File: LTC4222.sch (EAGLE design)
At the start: 29 parts, among them IC1 67997-100HLF, IC2 LTC4222, J1 PMV15ENEAR, J2 PMV15ENEAR

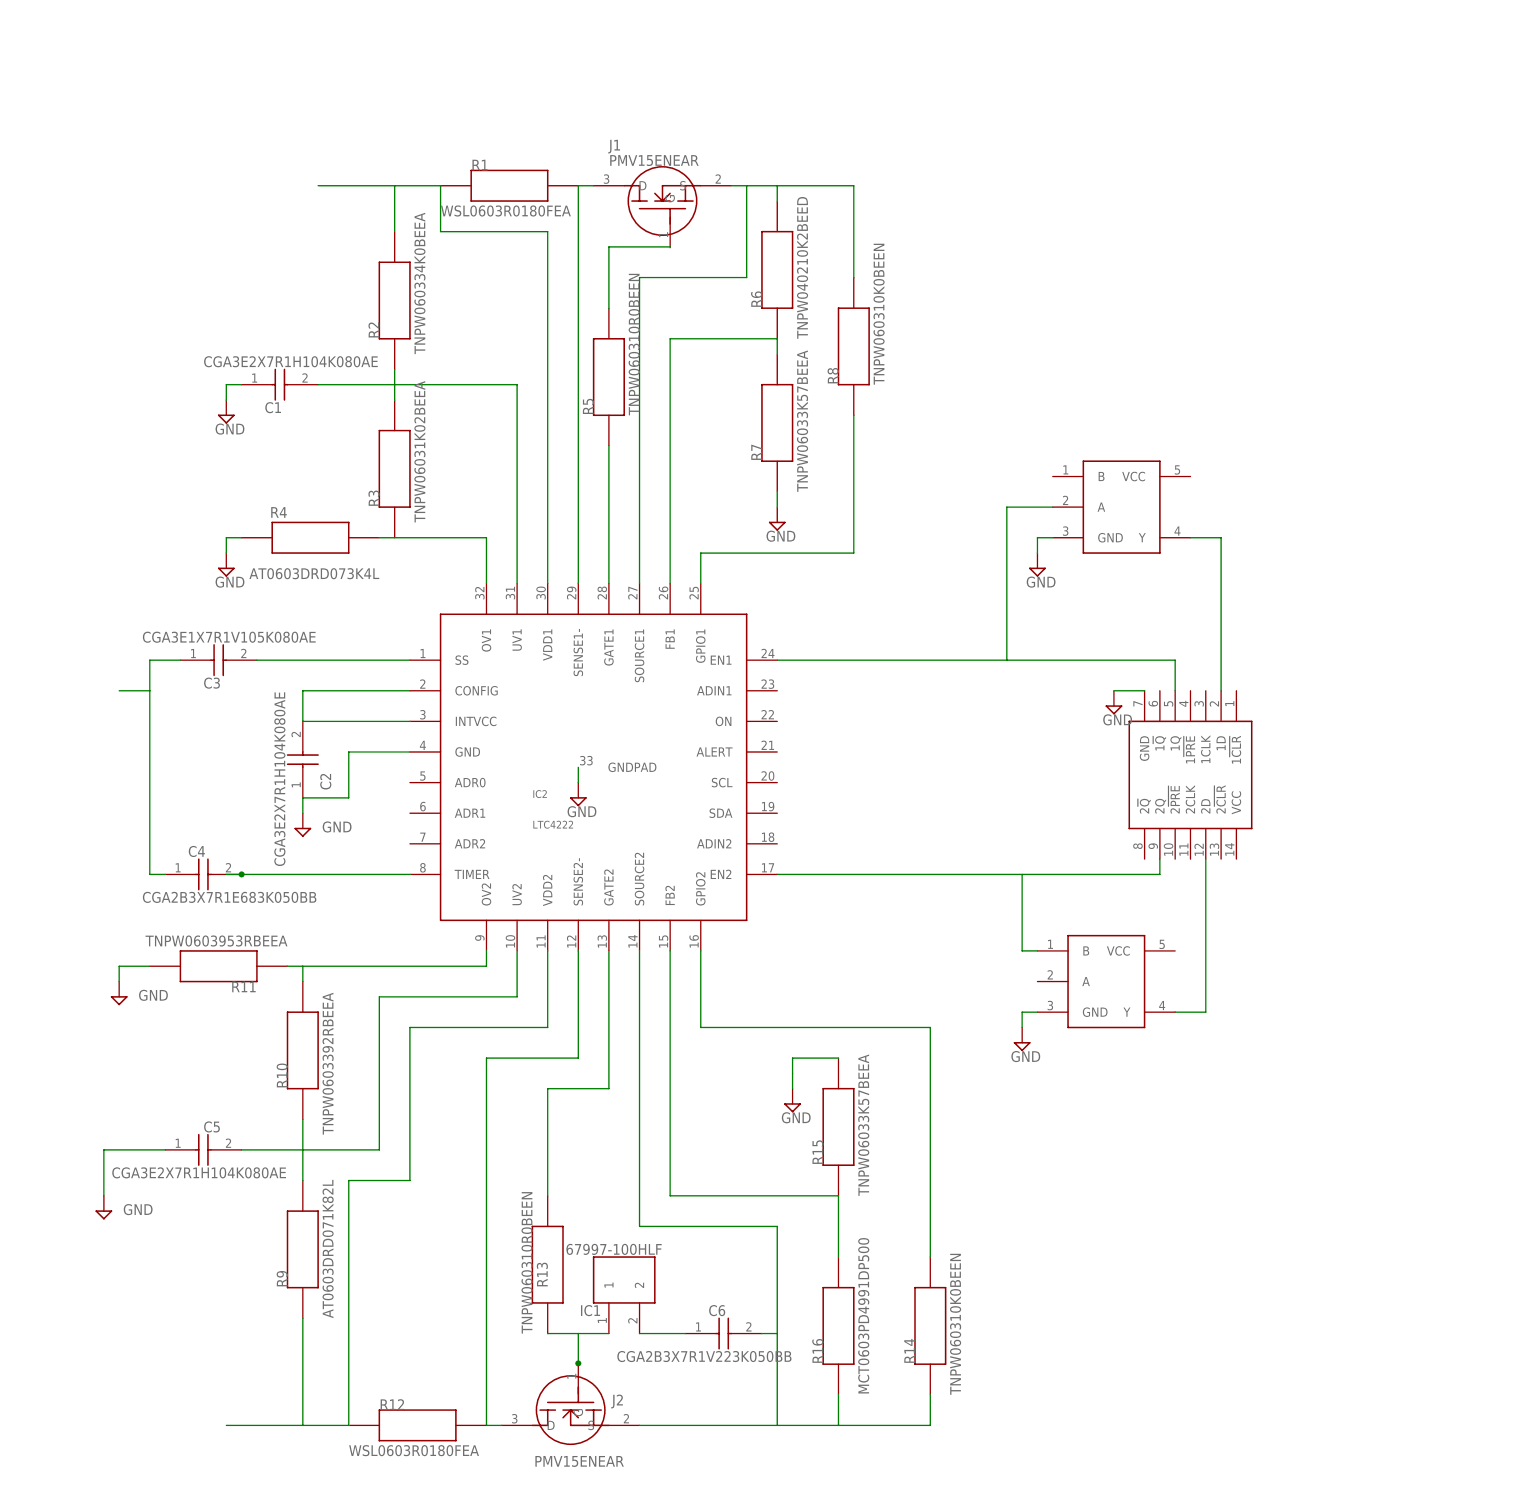
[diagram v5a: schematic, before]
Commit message: Polished LTC4222 schematic and added test points. Started on pin heads
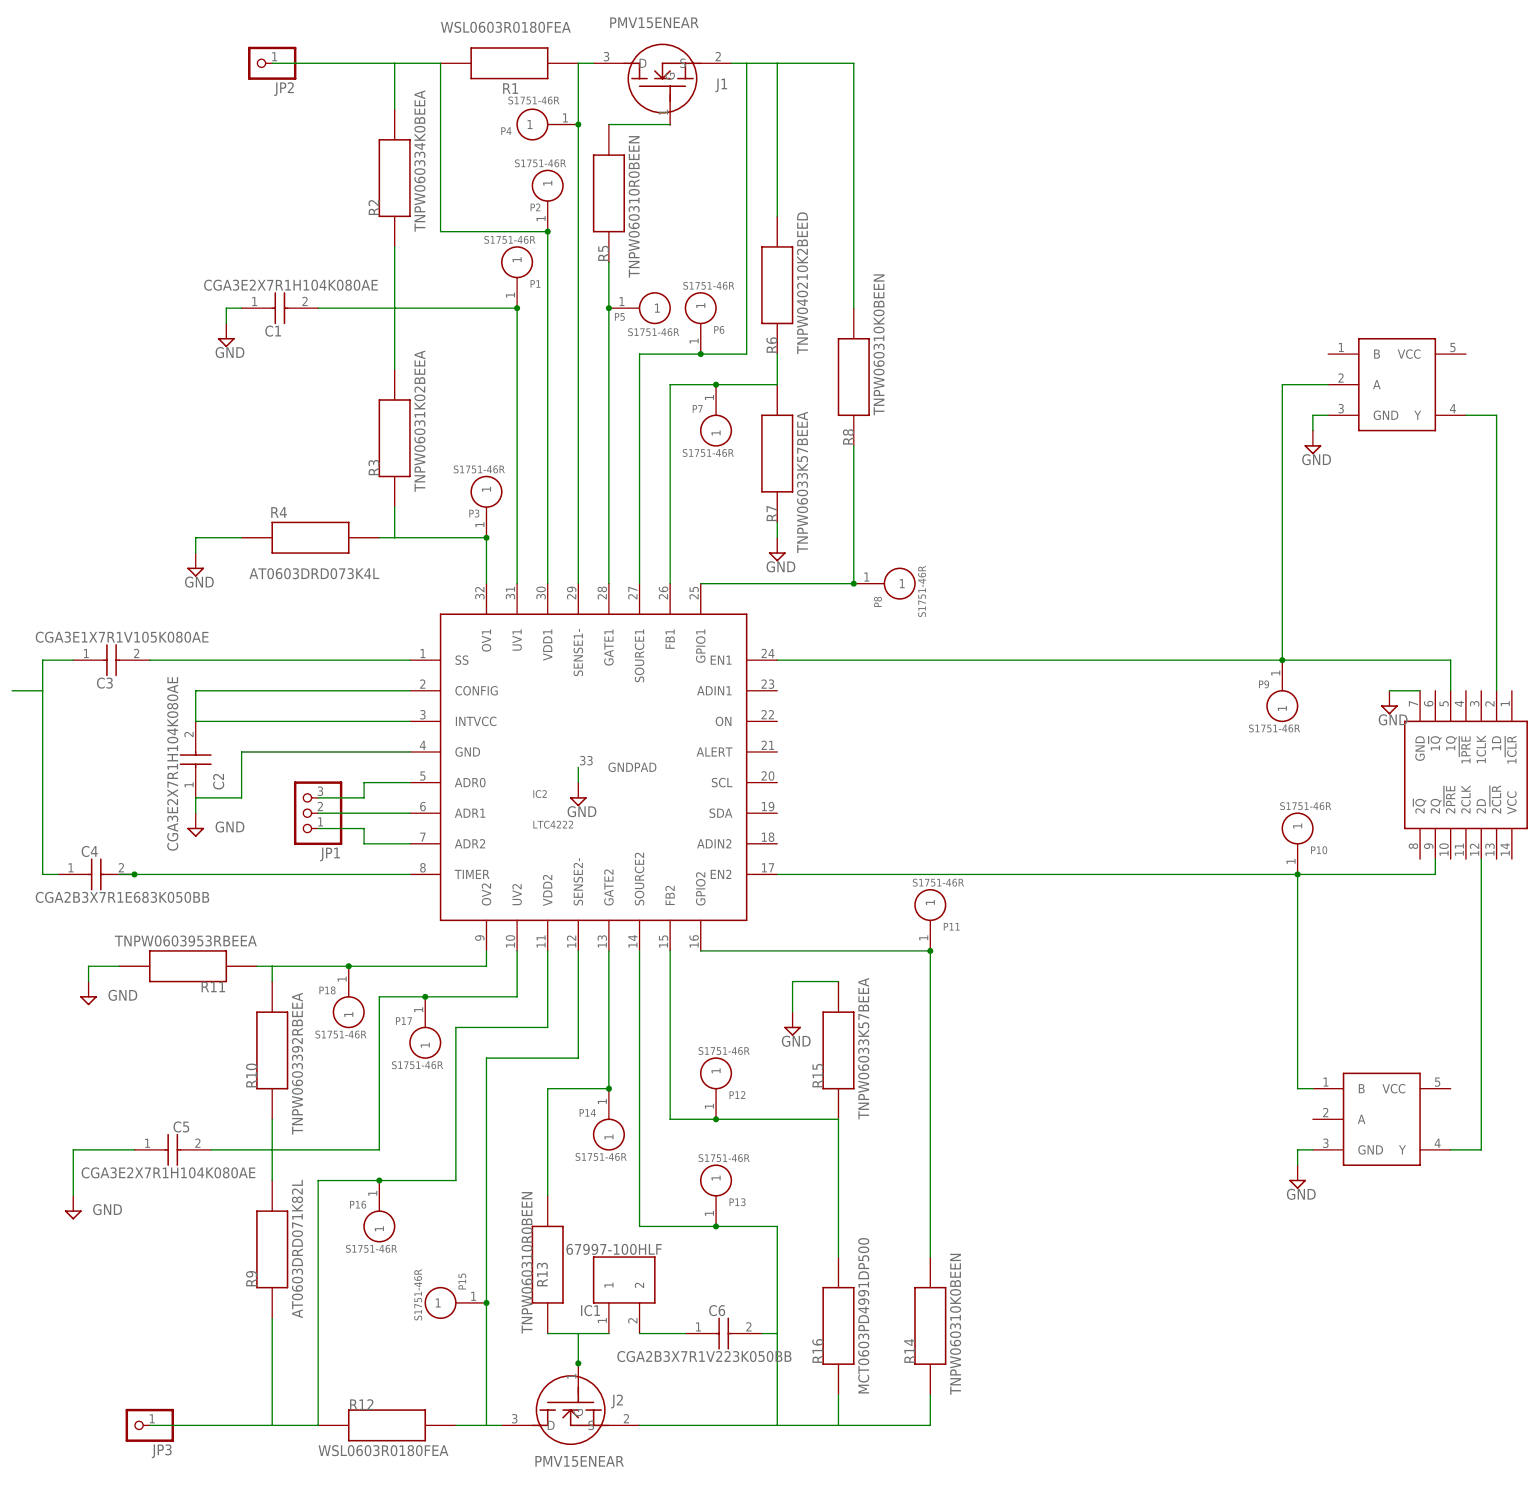
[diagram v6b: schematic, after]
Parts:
- added JP1: (no value), pinhead:PINHD-1X3
- added JP2, JP3: (no value), pinhead:PINHD-1X1
- added P1, P10, P11, P12, P13, P14, P15, P16, P17, P18, P2, P3, P4, P5, P6, P7, P8, P9: S1751-46R, Baja_Parts_Lib:S1751-46R
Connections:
- new net N$29: IC2.FB1, P7.1, R6.P$1, R7.P$2
- new net N$30: IC2.ADR1, JP1.2
- new net N$31: IC2.ADR0, JP1.3
- net N$11: now also P5.1
- net N$12: now also P6.1
- net N$13: now also IC2.ADR2, JP1.1; no longer IC2.FB1, R6.P$1, R7.P$2
- net N$14: now also P8.1
- net N$18: now also P14.1
- net N$19: now also P18.1
- net N$2: now also JP2.1, P2.1
- net N$20: now also P15.1
- net N$21: now also JP3.1, P16.1
- net N$23: now also P13.1
- net N$25: now also P12.1
- net N$26: now also P11.1
- net N$27: now also P17.1
- net N$3: now also P10.1
- net N$4: now also P9.1
- net N$6: now also P4.1
- net N$7: now also P3.1
- net N$8: now also P1.1
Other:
- moved on the sheet: C1, C2, C3, C4, C5, J1, R1, R10, R11, R12, R15, R2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

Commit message: LTC4222 V3; Finished up the headers; Need to source LEDs and LED resistors; Final step = MUX: Check up with Forrest about LDO after final step
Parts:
- added JP4: (no value), pinhead:PINHD-1X9
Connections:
- new net ADIN1: IC2.ADIN1, JP4.1
- new net ADIN2: IC2.ADIN2, JP4.4
- new net ALERT: IC2.ALERT, JP4.3
- new net A_OR_GATE#2: JP4.7, U$4.A
- new net B_OR_GATE#1: JP4.5, U$3.B
- new net ON: IC2.ON, JP4.2
- new net VCC_DFF: JP4.9, U$5.VCC
- new net VCC_OR_GATE#1: JP4.6, U$3.VCC
- new net VCC_OR_GATE#2: JP4.8, U$4.VCC
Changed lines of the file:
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@@
 <part name="JP2" library="pinhead" library_urn="urn:adsk.eagle:library:325" deviceset="PINHD-1X1" device="" package3d_urn="urn:adsk.eagle:package:22485/2"/>
 <part name="JP3" library="pinhead" library_urn="urn:adsk.eagle:library:325" deviceset="PINHD-1X1" device="" package3d_urn="urn:adsk.eagle:package:22485/2"/>
+<part name="JP4" library="pinhead" library_urn="urn:adsk.eagle:library:325" deviceset="PINHD-1X9" device="" package3d_urn="urn:adsk.eagle:package:22483/2"/>
 </parts>
 <sheets>
@@
 <attribute name="NAME" x="-191.77" y="-48.895" size="1.778" layer="95" rot="R180"/>
 <attribute name="VALUE" x="-191.77" y="-40.64" size="1.778" layer="96" rot="R180"/>
+</instance>
+<instance part="JP4" gate="A" x="71.12" y="66.04" smashed="yes">
+<attribute name="NAME" x="64.77" y="79.375" size="1.778" layer="95"/>
+<attribute name="VALUE" x="64.77" y="50.8" size="1.778" layer="96"/>
 </instance>
 </instances>
@@
 </segment>
 </net>
+<net name="A_OR_GATE#2" class="0">
+<segment>
+<pinref part="JP4" gate="A" pin="7"/>
+<wire x1="68.58" y1="60.96" x2="55.88" y2="60.96" width="0.1524" layer="91"/>
+<label x="38.1" y="60.96" size="1.778" layer="95"/>
+</segment>
+<segment>
+<pinref part="U$4" gate="G$1" pin="A"/>
+<wire x1="-2.54" y1="5.08" x2="-5.08" y2="5.08" width="0.1524" layer="91"/>
+<label x="-25.4" y="5.08" size="1.778" layer="95"/>
+</segment>
+</net>
+<net name="VCC_DFF" class="0">
+<segment>
+<pinref part="JP4" gate="A" pin="9"/>
+<wire x1="68.58" y1="55.88" x2="55.88" y2="55.88" width="0.1524" layer="91"/>
+<label x="43.18" y="55.88" size="1.778" layer="95"/>
+</segment>
+<segment>
+<pinref part="U$5" gate="G$1" pin="VCC"/>
+<wire x1="30.48" y1="48.26" x2="30.48" y2="43.18" width="0.1524" layer="91"/>
+<label x="30.48" y="40.64" size="1.778" layer="95"/>
+</segment>
+</net>
+<net name="VCC_OR_GATE#1" class="0">
+<segment>
+<pinref part="U$3" gate="G$1" pin="VCC"/>
+<wire x1="22.86" y1="132.08" x2="27.94" y2="132.08" width="0.1524" layer="91"/>
+<label x="30.48" y="132.08" size="1.778" layer="95"/>
+</segment>
+<segment>
+<pinref part="JP4" gate="A" pin="6"/>
+<wire x1="68.58" y1="63.5" x2="55.88" y2="63.5" width="0.1524" layer="91"/>
+<label x="35.56" y="63.5" size="1.778" layer="95"/>
+</segment>
+</net>
+<net name="B_OR_GATE#1" class="0">
+<segment>
+<pinref part="U$3" gate="G$1" pin="B"/>
+<wire x1="0" y1="132.08" x2="-7.62" y2="132.08" width="0.1524" layer="91"/>
+<label x="-25.4" y="132.08" size="1.778" layer="95"/>
+</segment>
+<segment>
+<pinref part="JP4" gate="A" pin="5"/>
+<wire x1="68.58" y1="66.04" x2="55.88" y2="66.04" width="0.1524" layer="91"/>
+<label x="38.1" y="66.04" size="1.778" layer="95"/>
+</segment>
+</net>
+<net name="VCC_OR_GATE#2" class="0">
+<segment>
+<pinref part="U$4" gate="G$1" pin="VCC"/>
+<wire x1="20.32" y1="10.16" x2="22.86" y2="10.16" width="0.1524" layer="91"/>
+<wire x1="22.86" y1="10.16" x2="22.86" y2="12.7" width="0.1524" layer="91"/>
+<label x="2.54" y="15.24" size="1.778" layer="95"/>
+</segment>
+<segment>
+<pinref part="JP4" gate="A" pin="8"/>
+<wire x1="68.58" y1="58.42" x2="55.88" y2="58.42" width="0.1524" layer="91"/>
+<label x="35.56" y="58.42" size="1.778" layer="95"/>
+</segment>
+</net>
+<net name="ADIN2" class="0">
+<segment>
+<pinref part="JP4" gate="A" pin="4"/>
+<wire x1="68.58" y1="68.58" x2="55.88" y2="68.58" width="0.1524" layer="91"/>
+<label x="48.26" y="68.58" size="1.778" layer="95"/>
+</segment>
+<segment>
+<pinref part="IC2" gate="G$1" pin="ADIN2"/>
+<wire x1="-91.44" y1="50.8" x2="-83.82" y2="50.8" width="0.1524" layer="91"/>
+<label x="-81.28" y="50.8" size="1.778" layer="95"/>
+</segment>
+</net>
+<net name="ALERT" class="0">
+<segment>
+<pinref part="IC2" gate="G$1" pin="ALERT"/>
+<wire x1="-91.44" y1="66.04" x2="-83.82" y2="66.04" width="0.1524" layer="91"/>
+<label x="-81.28" y="66.04" size="1.778" layer="95"/>
+</segment>
+<segment>
+<pinref part="JP4" gate="A" pin="3"/>
+<wire x1="68.58" y1="71.12" x2="55.88" y2="71.12" width="0.1524" layer="91"/>
+<label x="48.26" y="71.12" size="1.778" layer="95"/>
+</segment>
+</net>
+<net name="ON" class="0">
+<segment>
+<pinref part="IC2" gate="G$1" pin="ON"/>
+<wire x1="-91.44" y1="71.12" x2="-83.82" y2="71.12" width="0.1524" layer="91"/>
+<label x="-81.28" y="71.12" size="1.778" layer="95"/>
+</segment>
+<segment>
+<pinref part="JP4" gate="A" pin="2"/>
+<wire x1="68.58" y1="73.66" x2="55.88" y2="73.66" width="0.1524" layer="91"/>
+<label x="48.26" y="73.66" size="1.778" layer="95"/>
+</segment>
+</net>
+<net name="ADIN1" class="0">
+<segment>
+<pinref part="JP4" gate="A" pin="1"/>
+<wire x1="68.58" y1="76.2" x2="55.88" y2="76.2" width="0.1524" layer="91"/>
+<label x="48.26" y="76.2" size="1.778" layer="95"/>
+</segment>
+<segment>
+<pinref part="IC2" gate="G$1" pin="ADIN1"/>
+<wire x1="-91.44" y1="76.2" x2="-83.82" y2="76.2" width="0.1524" layer="91"/>
+<label x="-81.28" y="76.2" size="1.778" layer="95"/>
+</segment>
+</net>

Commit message: Began working on the PCB schematic and actually saving on git
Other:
- moved on the sheet: R5
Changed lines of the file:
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@@
 <attribute name="VALUE" x="-119.38" y="187.96" size="1.778" layer="96" rot="MR180"/>
 </instance>
-<instance part="R5" gate="G$1" x="-119.38" y="147.32" smashed="yes" rot="R90">
-<attribute name="NAME" x="-119.38" y="147.32" size="1.778" layer="95" rot="R90"/>
-<attribute name="VALUE" x="-114.3" y="144.78" size="1.778" layer="96" rot="R90"/>
+<instance part="R5" gate="G$1" x="-109.22" y="144.78" smashed="yes" rot="R90">
+<attribute name="NAME" x="-106.68" y="144.78" size="1.778" layer="95" rot="R90"/>
+<attribute name="VALUE" x="-104.14" y="142.24" size="1.778" layer="96" rot="R90"/>
 </instance>
 <instance part="R6" gate="G$1" x="-91.44" y="132.08" smashed="yes" rot="R90">
@@
 </instance>
 <instance part="IC2" gate="G$1" x="-147.32" y="38.1" smashed="yes">
-<attribute name="NAME" x="-132.08" y="58.42" size="1.27" layer="95"/>
-<attribute name="VALUE" x="-132.08" y="53.34" size="1.27" layer="96"/>
+<attribute name="NAME" x="-134.62" y="55.88" size="1.27" layer="95"/>
+<attribute name="VALUE" x="-134.62" y="50.8" size="1.27" layer="96"/>
 </instance>
 <instance part="SUPPLY11" gate="GND" x="-124.46" y="58.42" smashed="yes">
@@
 </segment>
 </net>
-<net name="N$9" class="0">
-<segment>
-<wire x1="-109.22" y1="170.18" x2="-119.38" y2="170.18" width="0.1524" layer="91"/>
-<pinref part="R5" gate="G$1" pin="P$2"/>
-</segment>
-</net>
 <net name="N$11" class="0">
 <segment>
 <pinref part="R5" gate="G$1" pin="P$1"/>
-<wire x1="-119.38" y1="147.32" x2="-119.38" y2="139.7" width="0.1524" layer="91"/>
+<wire x1="-109.22" y1="144.78" x2="-119.38" y2="139.7" width="0.1524" layer="91"/>
 <pinref part="IC2" gate="G$1" pin="GATE1"/>
 <pinref part="P5" gate="G$1" pin="1"/>
@@
 <wire x1="-129.54" y1="-30.48" x2="-124.46" y2="-30.48" width="0.1524" layer="91"/>
 <wire x1="-124.46" y1="-30.48" x2="-119.38" y2="-30.48" width="0.1524" layer="91"/>
-<wire x1="-124.46" y1="-35.56" x2="-124.46" y2="-35.43" width="0.1524" layer="91"/>
+<wire x1="-124.46" y1="-35.56" x2="-124.46" y2="-35.557" width="0.1524" layer="91"/>
 <pinref part="J2" gate="G$1" pin="G"/>
-<wire x1="-124.46" y1="-35.43" x2="-124.46" y2="-30.48" width="0.1524" layer="91"/>
-<junction x="-124.46" y="-35.43"/>
+<wire x1="-124.46" y1="-35.557" x2="-124.46" y2="-30.48" width="0.1524" layer="91"/>
+<junction x="-124.46" y="-35.557"/>
 </segment>
 </net>
@@
 </segment>
 </net>
+<net name="N$9" class="0">
+<segment>
+<pinref part="R5" gate="G$1" pin="P$2"/>
+<wire x1="-109.22" y1="167.64" x2="-109.22" y2="170.18" width="0.1524" layer="91"/>
+</segment>
+</net>
